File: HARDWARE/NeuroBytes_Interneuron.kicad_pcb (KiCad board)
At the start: 2 copper layers, 58.4 x 25 mm, 28 parts, among them P1 JST GH 4-POS, P2 JST GH 4-POS, P3 JST GH 4-POS, P4 JST GH 4-POS, P5 JST GH 4-POS, P6 JST GH 4-POS, P7 JST GH 4-POS, P8 JST GH 7-POS, Q1 NPN_dual, Q2 NPN_dual, SW1 SW_PUSH_TL3330AF130QG, U1 STM32L011Gx, U2 LD3985G33R

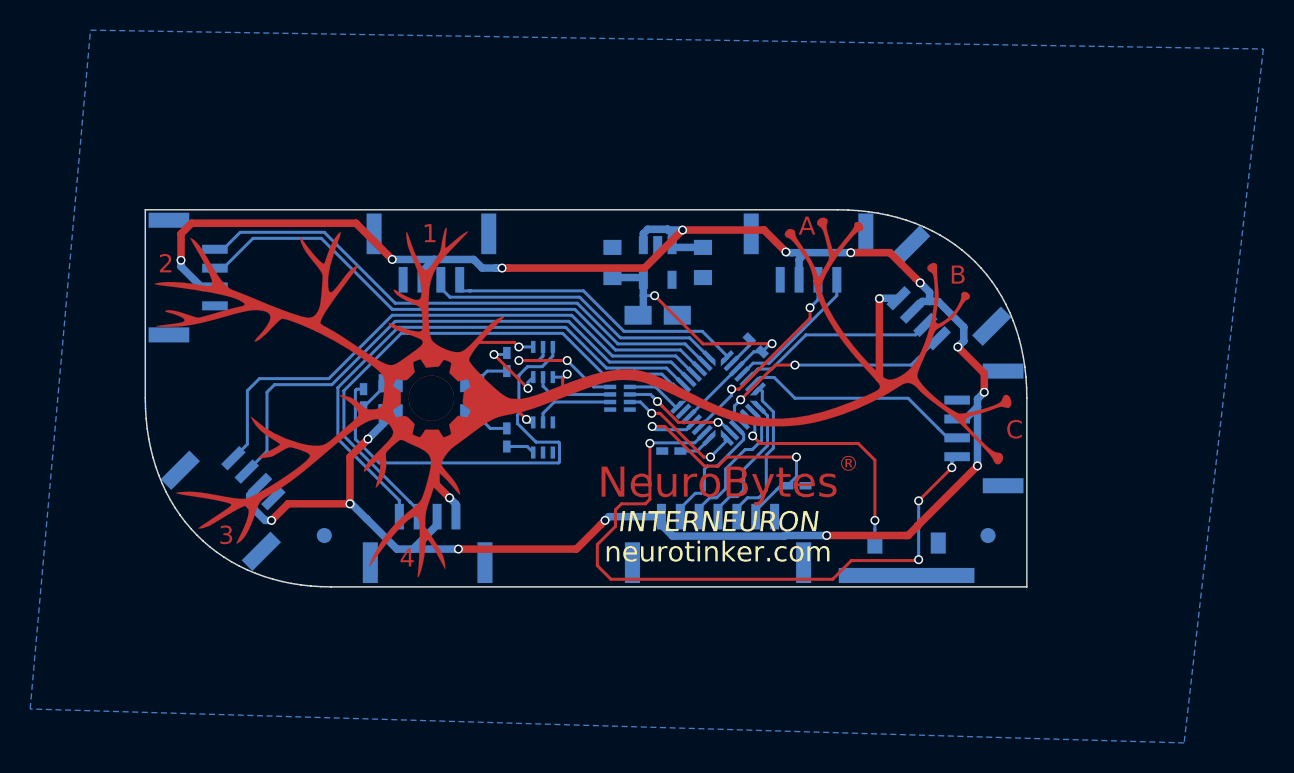
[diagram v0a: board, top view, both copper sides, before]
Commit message: Updated switch footprint (centered, removed part of support pad). Updated JST footprints (centered). BOM changes to reduce mfr cost: dual --> single NPN transistors; resistor network --> discrete resistors; 150 ohm --> 220 ohm resistor for red channel; different regulator; MLCC 10uF cap; etc
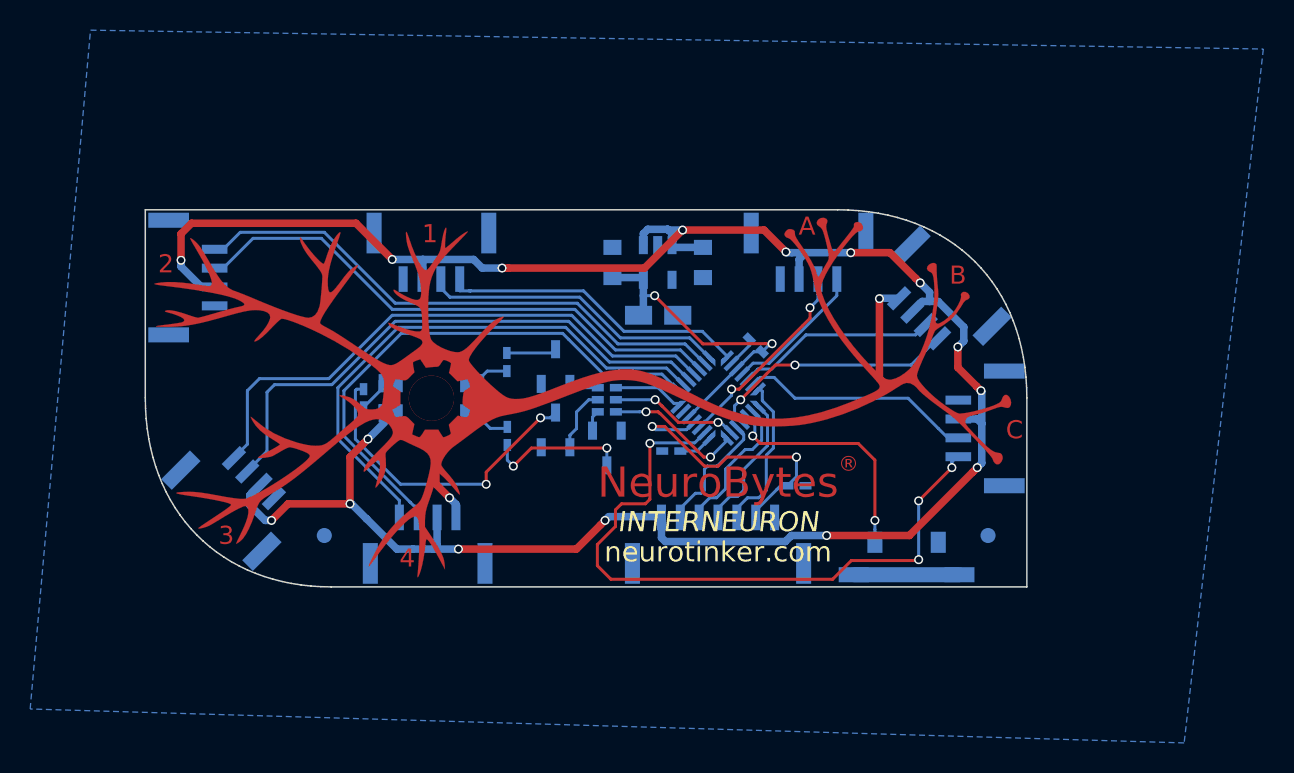
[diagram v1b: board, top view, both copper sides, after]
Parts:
- removed RN1: R_Pack04, KiCad_Footprints:ZF_RN_4iso_CTS-0804
- added Q3: MMBT3904, KiCad_Footprints:ZF_SOT23-3L, B.Cu at (158.2, 92.1)
- added R5: 1k, KiCad_Footprints:ZF_SMD_NonPol_0402, B.Cu at (161.6, 90.9)
- added R6: 1k, KiCad_Footprints:ZF_SMD_NonPol_0402, B.Cu at (161.6, 89.3)
- added R7: 1k, KiCad_Footprints:ZF_SMD_NonPol_0402, B.Cu at (161.6, 90.1)
- C2: footprint KiCad_Footprints:ZF_SMD_pol_1206 -> KiCad_Footprints:ZF_SMD_nonpol_1206
- Q1, Q2: value NPN_dual -> MMBT3904; footprint KiCad_Footprints:ZF_SMD_SOT-363 -> KiCad_Footprints:ZF_SOT23-3L
- R1: value 150 -> 220
- moved Q1 4.29 mm to (161.6, 93.3), turned to 180 degrees
- moved SW1 1.75 mm to (181.5, 100.5)
- moved Q2 0.88 mm to (158.2, 87.9), turned to 0 degrees
- moved P8 0.75 mm to (169.0, 99.5)
- moved P3 0.73 mm to (137.0, 96.5)
- moved P7 0.69 mm to (183.5, 83.5)
- moved P2 0.68 mm to (133.9, 82.0)
- moved P1 0.65 mm to (150.0, 80.4)
- moved P4 0.65 mm to (149.8, 99.6)
- moved P6 0.65 mm to (175.0, 80.4)
- moved P5 0.62 mm to (186.6, 92.0)
- moved R1 0.10 mm to (155.0, 92.5)
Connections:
- P1 pad : (no net) -> GND
- P2 pad : (no net) -> GND
- P3 pad : (no net) -> GND
- P4 pad : (no net) -> GND
- P5 pad : (no net) -> GND
- P6 pad : (no net) -> GND
- P7 pad : (no net) -> GND
- P8 pad : (no net) -> GND
- Q1 pad 1: GND -> Net-(Q1-Pad1)
- Q1 pad 2: Net-(Q1-Pad2) -> GND
- Q2 pad 1: GND -> Net-(Q2-Pad1)
- Q2 pad 2: Net-(Q2-Pad2) -> GND
- R1 pad 2: Net-(Q1-Pad6) -> Net-(Q1-Pad3)
- R3 pad 2: Net-(Q2-Pad6) -> Net-(Q3-Pad3)
- SW1 pad : (no net) -> GND
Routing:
- net Net-(Q2-Pad6): track 29.2 -> 0.00 mm
- net Net-(Q3-Pad3): track 0.00 -> 20.7 mm, vias 0 -> 2
- net GND: track 38.0 -> 20.4 mm, vias 5 -> 2
- net Net-(Q1-Pad3): track 0.00 -> 9.56 mm, vias 0 -> 2
- net Net-(Q2-Pad5): track 9.35 -> 0.00 mm, vias 2 -> 0
- net Net-(Q1-Pad2): track 5.36 -> 0.00 mm
- net Net-(Q2-Pad2): track 5.28 -> 0.00 mm
- net Net-(Q3-Pad1): track 0.00 -> 4.27 mm
- net Net-(Q2-Pad1): track 0.00 -> 1.95 mm
- net Net-(Q1-Pad6): track 1.92 -> 0.00 mm
- net +5V: track 153.0 -> 154.9 mm
- net Net-(Q2-Pad3): track 5.27 -> 3.47 mm, vias 2 -> 0
- net Net-(Q1-Pad1): track 0.00 -> 1.39 mm
- net LED_G: track 3.67 -> 4.73 mm
- net LED_B: track 7.86 -> 8.64 mm
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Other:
- net class Default: clearance 0.19 -> 0.2
- rule trace_clearance: 0.19 -> 0.2

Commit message: Updated PCB outline to eliminate rotational symmetry. Changed to 5-pin JST GH connector for power. Numerous routing changes and minor graphics updates.
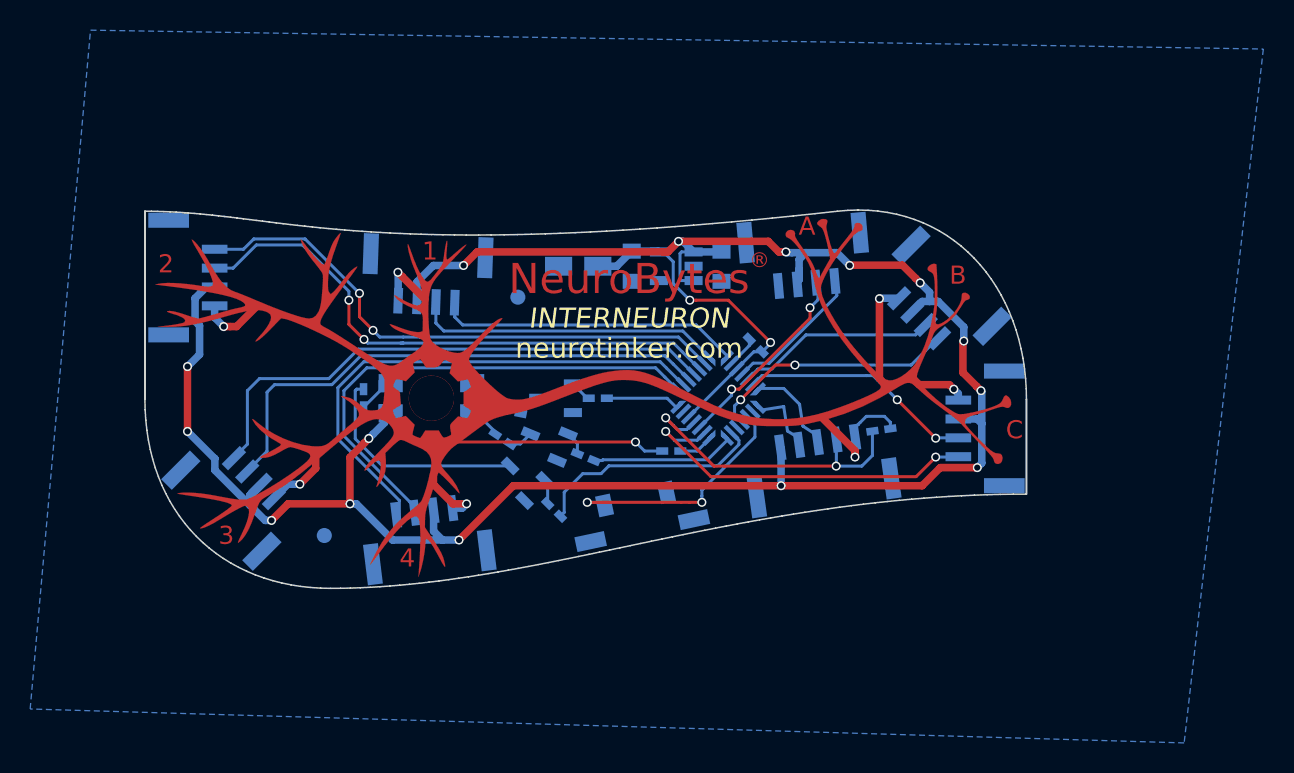
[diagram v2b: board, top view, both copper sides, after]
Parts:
- P8: value JST GH 7-POS -> JST_GH_5-pos; footprint KiCad_Footprints:ZF_CONN_JST_GH_7POS -> KiCad_Footprints:ZF_CONN_JST_GH_5POS
- U2: value LD3985G33R -> TLV702
- moved REF** 34.9 mm to (155.7, 83.3)
- moved SW1 18.0 mm to (163.7, 97.6), turned to 192 degrees
- moved P8 8.46 mm to (175.8, 94.5), turned to 278 degrees
- moved R7 8.10 mm to (158.1, 97.4), turned to 315 degrees
- moved C5 6.74 mm to (179.8, 92.1), turned to 8 degrees
- moved C2 6.22 mm to (159.7, 81.2), turned to 180 degrees
- moved Q1 4.03 mm to (157.6, 92.8), turned to 67.5 degrees
- moved Q3 3.88 mm to (156.0, 95.3), turned to 45 degrees
- moved R2 3.32 mm to (155.3, 90.9), turned to 348.7 degrees
- moved R5 3.31 mm to (160.2, 93.9), turned to 337.5 degrees
- moved Q2 2.10 mm to (158.2, 90.0), turned to 90 degrees
- moved P1 1.52 mm to (149.7, 81.9), turned to 88 degrees
- moved C4 1.30 mm to (163.3, 81.2), turned to 270 degrees
- moved C1 1.26 mm to (169.2, 81.2)
- moved U2 1.26 mm to (166.2, 81.2), turned to 270 degrees
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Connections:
- net SWCLK/MISO renamed SWCLK
- net SWDIO/SCK renamed SWDIO
- P8 pad 5: NSS -> +5V
- U1 pad 23: NSS -> Net-(U1-Pad23)
- U1 pad 26: MOSI -> Net-(U1-Pad26)
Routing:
- net GND: track 20.4 -> 56.9 mm, vias 2 -> 8
- net A3EX: track 45.2 -> 24.9 mm, vias 4 -> 2
- net NSS: track 9.48 -> 0.00 mm
- net MOSI: track 8.45 -> 0.00 mm
- net +5V: track 154.9 -> 146.7 mm, vias 16 -> 15
- net Net-(Q1-Pad3): track 9.56 -> 1.62 mm, vias 2 -> 0
- net LED_B: track 8.64 -> 15.6 mm, vias 2 -> 0
- net Net-(Q3-Pad3): track 20.7 -> 14.9 mm, vias 2 -> 0
- net SWCLK: track 9.50 -> 5.13 mm
- net D4IN: track 36.1 -> 33.2 mm
- net Net-(Q3-Pad1): track 4.27 -> 1.61 mm
- net SWDIO: track 10.3 -> 8.00 mm
- net Net-(Q2-Pad3): track 3.47 -> 1.48 mm
- net RESET: track 19.4 -> 21.4 mm
- net D4EX: track 36.4 -> 34.5 mm
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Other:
- board size 58.4 x 25 mm -> 58.4 x 25.1 mm

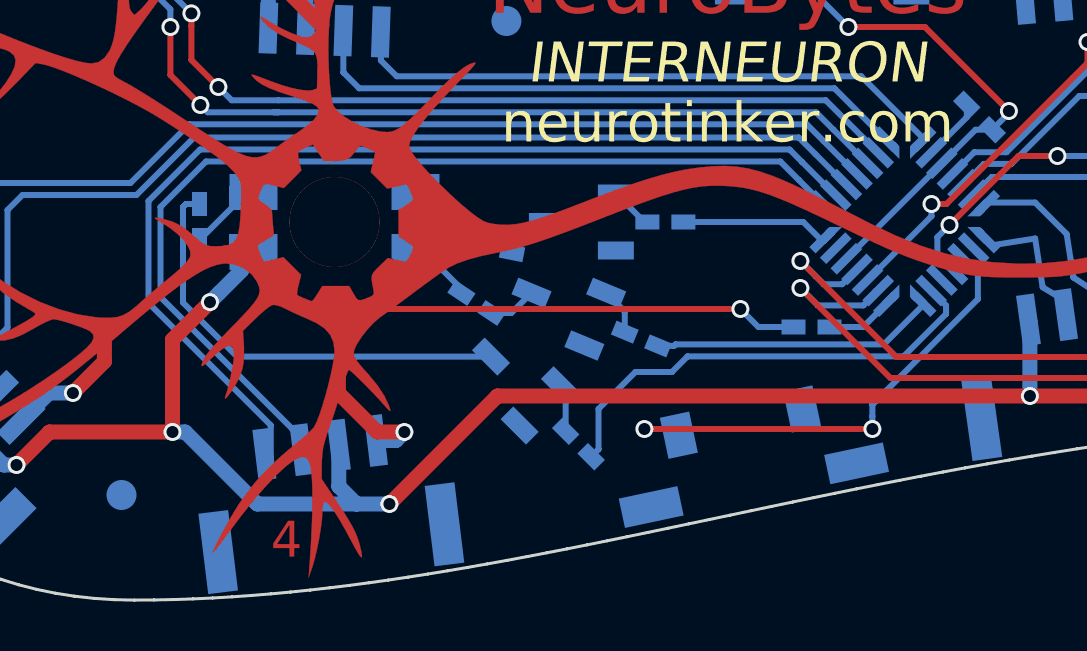
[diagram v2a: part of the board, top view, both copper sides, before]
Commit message: moved transistors around a bit so they don't overlap anymore.
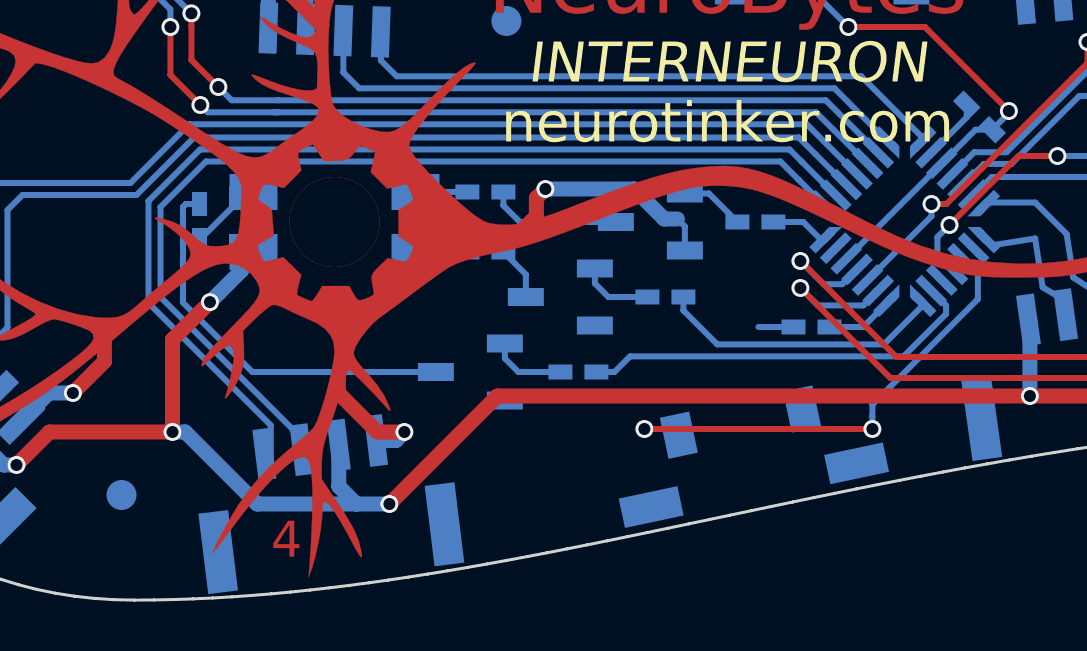
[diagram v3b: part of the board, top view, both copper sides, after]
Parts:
- moved R6 3.00 mm to (164.0, 90.0)
- moved R7 2.40 mm to (158.1, 95.0), turned to 0 degrees
- moved Q2 2.30 mm to (160.5, 90.0)
- moved R2 1.92 mm to (155.0, 89.0), turned to 0 degrees
- moved R1 1.73 mm to (155.0, 91.0), turned to 0 degrees
- moved R5 1.61 mm to (161.0, 92.5), turned to 0 degrees
- moved Q3 1.53 mm to (154.5, 95.0), turned to 90 degrees
- moved Q1 0.32 mm to (157.5, 92.5), turned to 90 degrees
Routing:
- net GND: track 56.9 -> 51.1 mm
- net LED_G: track 4.88 -> 1.88 mm
- net Net-(Q2-Pad3): track 1.48 -> 4.43 mm
- net LED_B: track 15.6 -> 13.4 mm
- net Net-(Q3-Pad3): track 14.9 -> 13.3 mm
- net Net-(D1-Pad4): track 2.50 -> 1.47 mm
- net Net-(Q3-Pad1): track 1.61 -> 2.54 mm
- net Net-(Q1-Pad1): track 1.56 -> 2.44 mm
- net Net-(Q2-Pad1): track 1.44 -> 2.14 mm
